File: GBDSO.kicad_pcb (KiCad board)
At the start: 2 copper layers, 85 x 61 mm, 78 parts, among them J1 MJ-3523-SMT-TR, J2 MJ-3523-SMT-TR, J3 EdgeConnector, J4 GameBoy Cartridge Connector, P1 100k, P2 100k, SW1 SW_SPDT, SW2 SW_SPDT, U1 TL062, U10 AT27C256R-PDIP28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

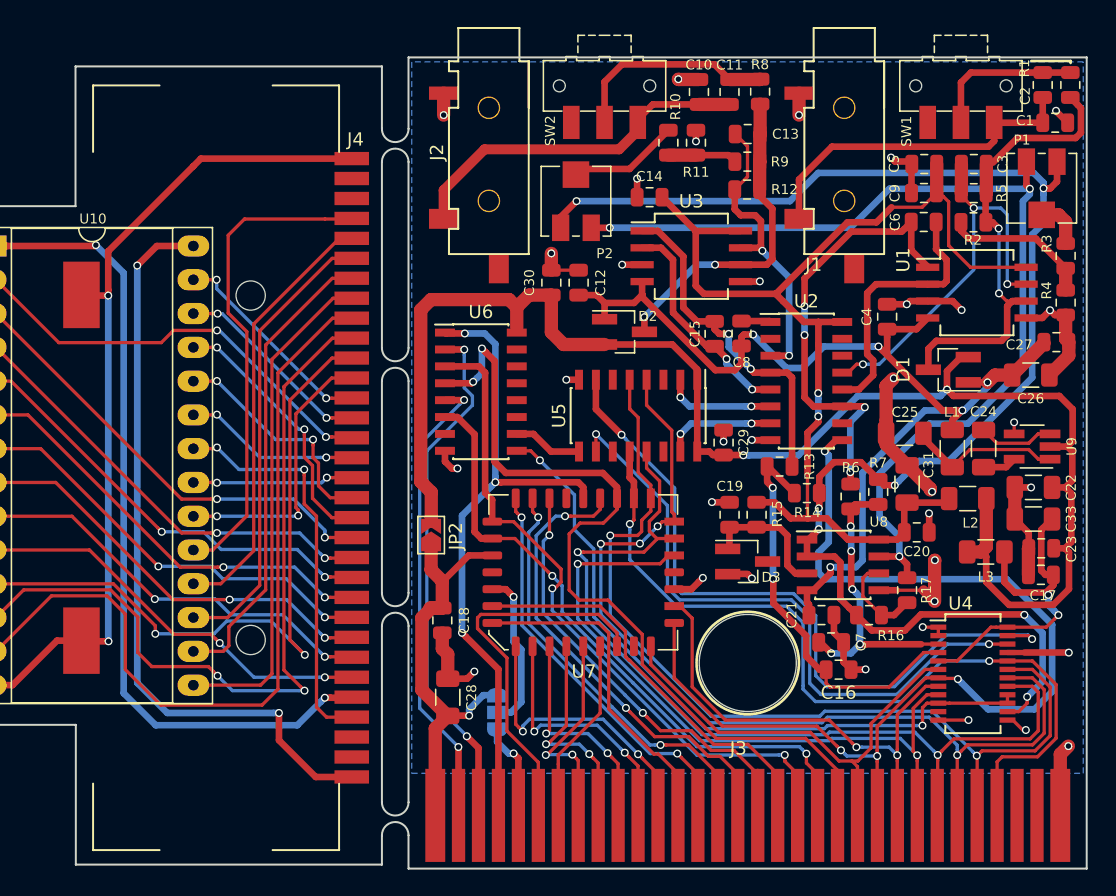
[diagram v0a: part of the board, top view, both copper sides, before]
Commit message: modify PCB to match the cart dimensions, update all gerber files, update PCB pictures
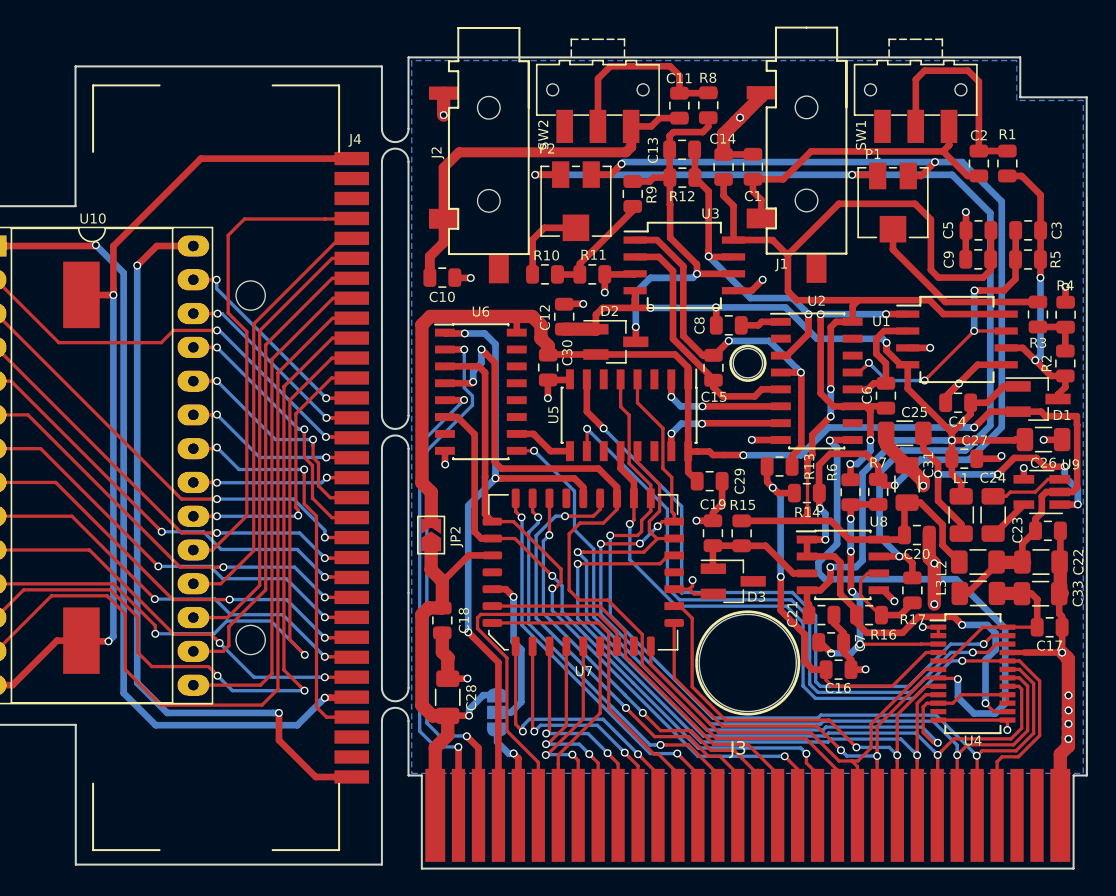
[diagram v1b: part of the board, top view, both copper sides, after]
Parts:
- moved C10 23.8 mm to (83.3, 107.7), turned to 0 degrees
- moved C1 23.0 mm to (106.7, 99.4), turned to 90 degrees
- moved R10 13.6 mm to (91.0, 107.5), turned to 0 degrees
- moved C6 13.4 mm to (116.7, 116.6), turned to 270 degrees
- moved R2 12.7 mm to (130.2, 114.2), turned to 270 degrees
- moved R11 12.6 mm to (94.6, 107.5), turned to 180 degrees
- moved P1 11.2 mm to (117.2, 102.1)
- moved C27 11.2 mm to (122.5, 121.3)
- moved R9 8.95 mm to (97.6, 101.4), turned to 90 degrees
- moved C4 8.39 mm to (122.1, 117.1), turned to 0 degrees
- moved C2 7.61 mm to (123.7, 99.1)
- moved R1 7.57 mm to (125.8, 99.1)
- moved D1 7.10 mm to (128.1, 116.8), turned to 0 degrees
- moved C3 6.45 mm to (127.4, 104.2)
- moved C5 6.45 mm to (123.6, 104.2)
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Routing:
- net +5V: track 154.9 -> 134.4 mm
- net Net-(C3-Pad1): track 36.5 -> 23.0 mm
- net Net-(C25-Pad1): track 11.7 -> 24.1 mm, vias 0 -> 4
- net Net-(C6-Pad1): track 20.3 -> 8.58 mm
- net +5VC: track 25.1 -> 14.0 mm, vias 2 -> 0
- net Net-(P1-Pad2): track 3.64 -> 14.1 mm
- net Net-(C3-Pad2): track 32.8 -> 23.6 mm, vias 3 -> 4
- net Net-(C6-Pad2): track 33.7 -> 24.8 mm
- net +2.5V: track 113.7 -> 104.8 mm
- net +5VA: track 87.0 -> 95.5 mm
- net Net-(R2-Pad1): track 11.5 -> 3.84 mm
- net GND: track 170.3 -> 177.6 mm, vias 36 -> 33
- net Net-(C13-Pad1): track 24.6 -> 29.6 mm
- net Net-(C2-Pad2): track 11.5 -> 15.9 mm
- net /GBDSO Cartridge/D1: track 80.1 -> 75.7 mm
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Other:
- board size 85 x 61 mm -> 85.1 x 61 mm

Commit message: minor updates
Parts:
- moved C1 61.5 mm to (164.3, 77.9)
- moved C11 61.5 mm to (158.8, 73.3)
- moved C12 61.5 mm to (150.1, 89.1)
- moved C13 61.5 mm to (159.0, 76.6)
- moved C15 61.5 mm to (161.3, 93.0)
- moved C19 61.5 mm to (161.3, 105.4)
- moved C2 61.5 mm to (181.3, 77.6)
- moved C21 61.5 mm to (169.5, 111.6)
- moved C22 61.5 mm to (186.0, 107.6)
- moved C23 61.5 mm to (186.5, 105.2)
- moved C26 61.5 mm to (186.2, 98.4)
- moved C28 61.5 mm to (141.4, 117.8)
- moved C29 61.5 mm to (161.1, 101.5)
- moved C31 61.5 mm to (175.9, 101.7)
- moved C33 61.5 mm to (185.9, 110.0)
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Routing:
- net GND: track 177.6 -> 182.1 mm, vias 33 -> 32
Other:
- board size 85.1 x 61 mm -> 85 x 61 mm

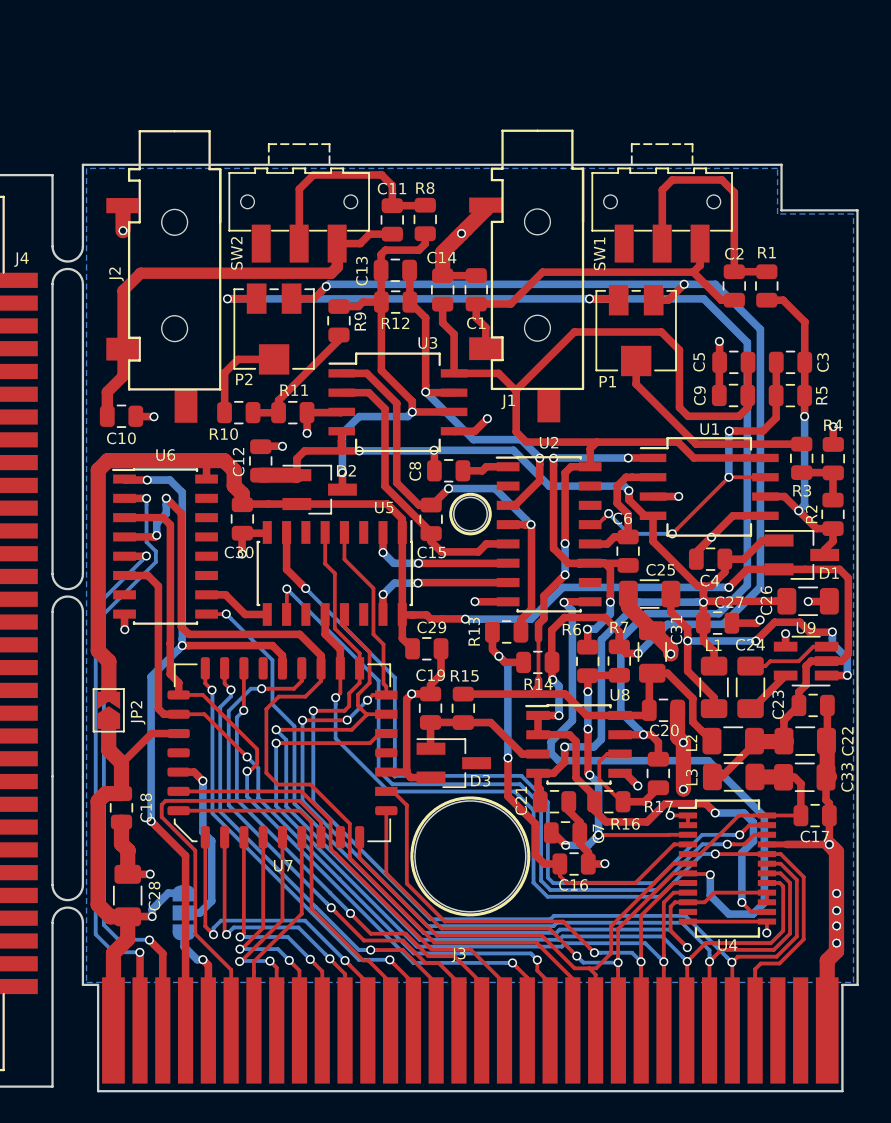
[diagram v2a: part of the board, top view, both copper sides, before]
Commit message: Bunch of changes: fixed pin swap on DS1267_SOIC, fixed footprint of all uncorrect ICs, fixed footprint off the three inductors as they were too big. Because of the size change of the footprint of the ICs, some components had to be rearranged. Some routing improvements have been done, mostly on the right side of the board. I've added header pins to each channel input so that if anyone wants to use those instead of a 3.5mm audio jack they can. I've also added a few vias to the 3.5mm audio jack connectors and switches to hopefully help with mechanical stresses due to usage. That's all I can remember, should have split it into multiple commits...
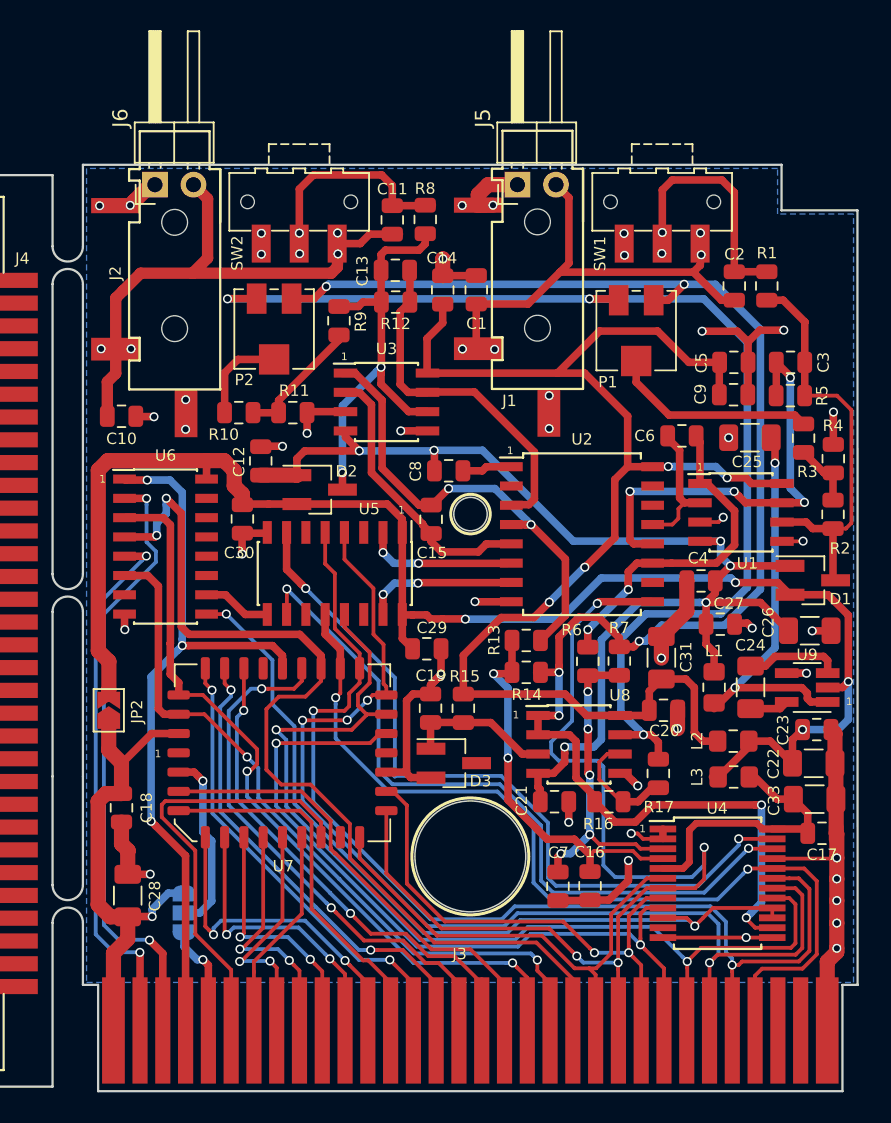
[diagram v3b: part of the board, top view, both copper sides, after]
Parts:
- added J5: Conn_01x02, Connector_PinHeader_2.54mm:PinHeader_1x02_P2.54mm_Horizontal, F.Cu at (167.0, 70.9)
- added J6: Conn_01x02, Connector_PinHeader_2.54mm:PinHeader_1x02_P2.54mm_Horizontal, F.Cu at (143.2, 70.9)
- L1, L2, L3: footprint Inductor_SMD:L_1206_3216Metric -> Inductor_SMD:L_0805_2012Metric_Pad1.15x1.40mm_HandSolder
- U1, U3: footprint Package_SO:SO-8_5.3x6.2mm_P1.27mm -> Package_SO:SOIC-8_3.9x4.9mm_P1.27mm
- U2: footprint Package_SO:SOIC-16_3.9x9.9mm_P1.27mm -> Package_SO:SOIC-16W_7.5x10.3mm_P1.27mm
- U4: footprint Package_SO:SSOP-24_3.9x8.7mm_P0.635mm -> Package_SO:SSOP-24_5.3x8.2mm_P0.65mm
- moved C25 12.2 mm to (182.3, 87.6)
- moved C6 8.38 mm to (177.8, 87.5), turned to 0 degrees
- moved C7 3.55 mm to (169.7, 117.1), turned to 270 degrees
- moved U1 2.68 mm to (181.7, 92.5)
- moved U2 2.16 mm to (171.3, 94.0)
- moved C26 1.94 mm to (186.3, 100.3)
- moved D1 1.82 mm to (186.5, 97.0)
- moved C16 1.78 mm to (171.8, 117.1), turned to 270 degrees
- moved U9 1.74 mm to (186.1, 104.0)
- moved C23 1.61 mm to (186.7, 106.8)
- moved C33 1.58 mm to (186.6, 111.4)
- moved C22 1.56 mm to (186.5, 109.0)
- moved C4 1.56 mm to (179.1, 97.0)
- moved R13 1.40 mm to (167.6, 101.0)
- moved R3 1.34 mm to (185.9, 87.6)
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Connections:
- U2 pad 12: Net-(C6-Pad1) -> Net-(C3-Pad2)
- U2 pad 13: Net-(C3-Pad2) -> Net-(C6-Pad1)
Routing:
- net Net-(C10-Pad1): track 30.0 -> 38.4 mm, vias 0 -> 4
- net Net-(C1-Pad1): track 24.3 -> 31.8 mm, vias 0 -> 4
- net Net-(C3-Pad2): track 23.6 -> 28.8 mm
- net +5VA: track 95.5 -> 91.0 mm, vias 2 -> 4
- net Net-(C16-Pad1): track 30.0 -> 25.7 mm
- net Net-(C3-Pad1): track 23.0 -> 27.3 mm, vias 2 -> 0
- net /GBDSO Cartridge/D1: track 75.7 -> 71.6 mm
- net +5VC: track 14.0 -> 18.1 mm
- net /GBDSO Cartridge/D5: track 70.8 -> 74.1 mm
- net GND: track 182.1 -> 185.2 mm, vias 32 -> 37
- net /GBDSO Cartridge/D6: track 68.8 -> 71.8 mm
- net Net-(C6-Pad2): track 24.8 -> 22.4 mm, vias 4 -> 2
- net Net-(C25-Pad1): track 24.1 -> 26.3 mm, vias 4 -> 2
- net +5V: track 134.4 -> 136.7 mm, vias 3 -> 5
- net /GBDSO Cartridge/D2: track 35.9 -> 33.9 mm
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
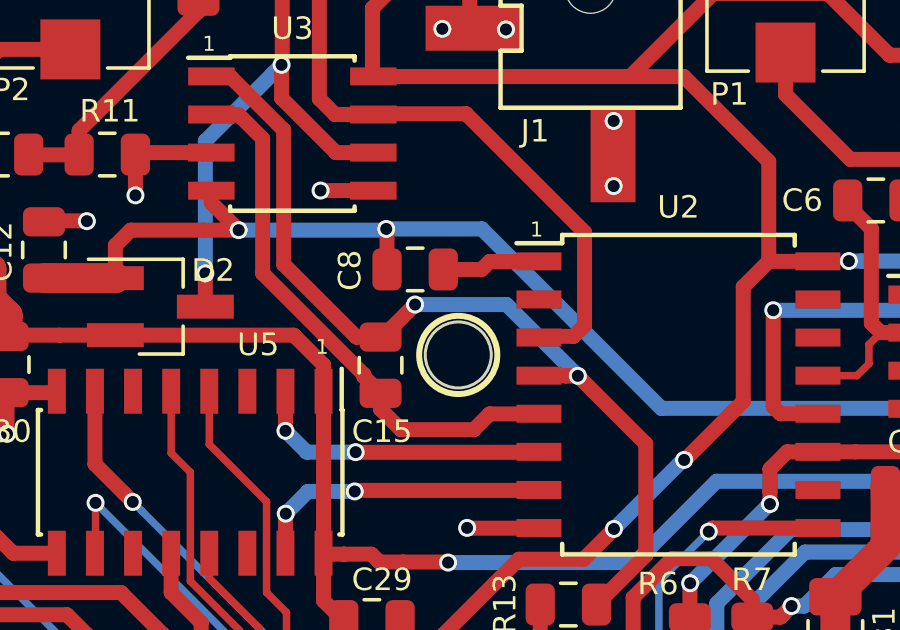
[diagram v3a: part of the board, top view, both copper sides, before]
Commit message: Moved small hole to correct position, also had to move C8 and the -5V trace because of the hole.
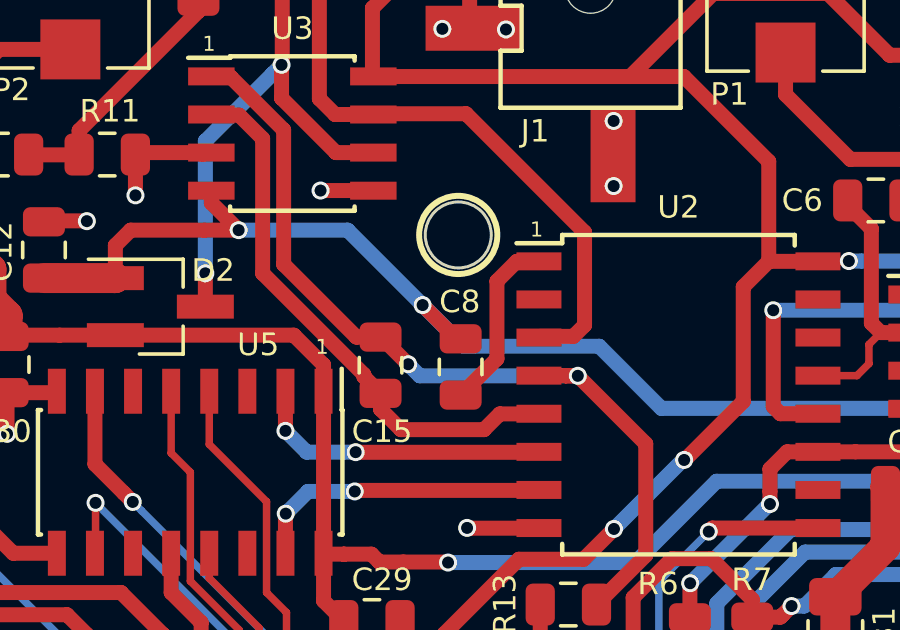
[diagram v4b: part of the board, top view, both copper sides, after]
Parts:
- moved C8 3.59 mm to (164.0, 93.0), turned to 90 degrees
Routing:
- net Net-(C8-Pad1): track 3.09 -> 5.97 mm
- net Net-(C15-Pad1): track 31.2 -> 30.3 mm
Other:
- outline, holes or cut-outs redrawn

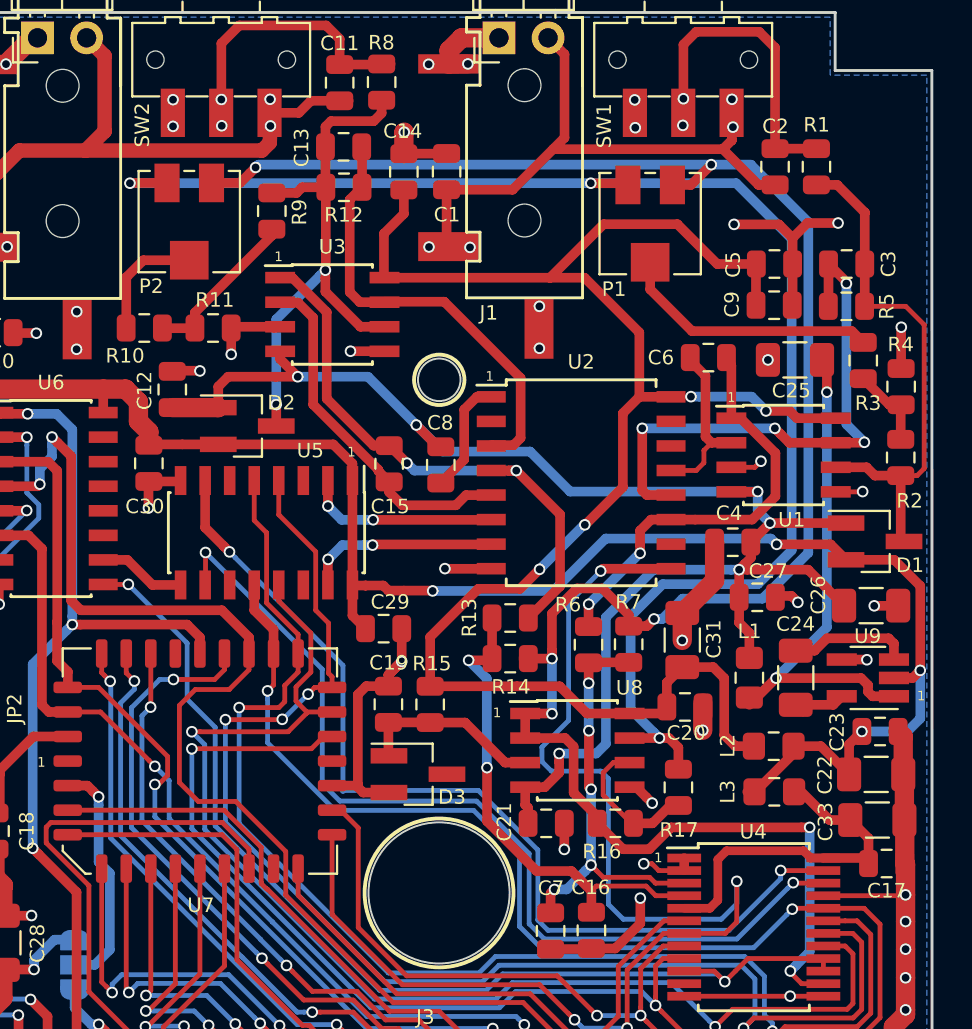
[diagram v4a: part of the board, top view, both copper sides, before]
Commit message: updated gerber files with latest fixes/improvements to the PCB
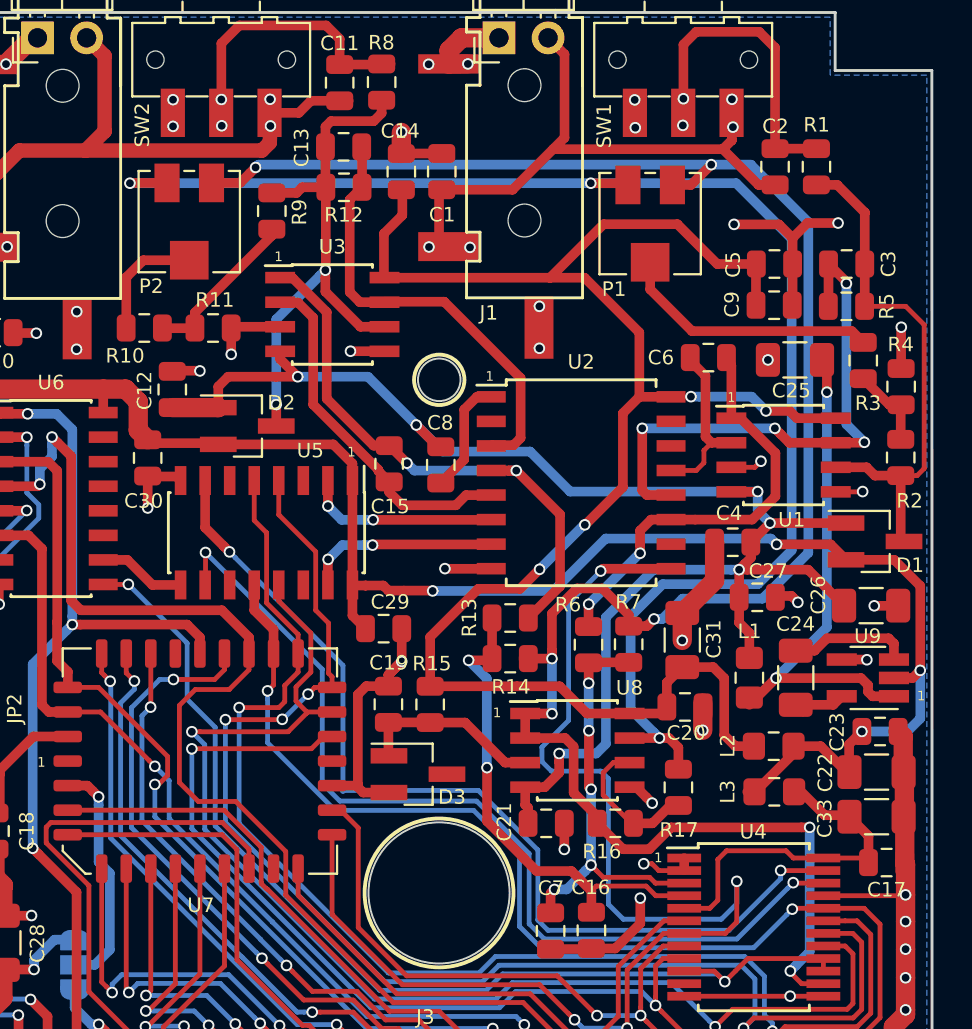
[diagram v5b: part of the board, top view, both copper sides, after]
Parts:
- moved C30 0.29 mm to (148.8, 92.7)
- moved C1 0.25 mm to (164.1, 77.9)
- moved C33 0.17 mm to (186.6, 111.2)
- moved C14 0.13 mm to (162.0, 77.9)
- moved C22 0.12 mm to (186.6, 108.9)
- moved C17 0.05 mm to (187.1, 113.6)
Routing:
- net Net-(C1-Pad1): track 31.8 -> 32.3 mm
